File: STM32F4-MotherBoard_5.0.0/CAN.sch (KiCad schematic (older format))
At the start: 0 parts

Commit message: SDとCANの追加とラベルミス修正
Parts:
- added J? (x2): RJ45, symbol RJ45
- added R?: 10k, symbol R
- added U?: MCP2551-I/SN, SO-8, symbol MCP2551-I/SN
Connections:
- net labels added: CAN_RX, CAN_TX, GND
- wire segments 0 -> 47
- no-connect marks 0 -> 1
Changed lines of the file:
@@
 $Descr A4 11693 8268
 encoding utf-8
-Sheet 3 10
+Sheet 3 11
 Title ""
 Date ""
@@
 Comment4 ""
 $EndDescr
+$Comp
+L MCP2551-I/SN U?
+U 1 1 58A2CD9A
+P 5450 3500
+F 0 "U?" H 5050 3850 50  0000 L CNN
+F 1 "MCP2551-I/SN" H 5550 3850 50  0000 L CNN
+F 2 "SO-8" H 5450 3500 50  0000 C CIN
+F 3 "" H 5450 3500 50  0000 C CNN
+	1    5450 3500
+	1    0    0    -1
+$EndComp
+Text GLabel 4500 3400 0    60   Input ~ 0
+CAN_TX
+Text GLabel 4500 3300 0    60   Input ~ 0
+CAN_RX
+Wire Wire Line
+	4500 3300 4950 3300
+Wire Wire Line
+	4950 3400 4500 3400
+$Comp
+L RJ45 J?
+U 1 1 58A2F3E9
+P 7200 2750
+F 0 "J?" H 7400 3250 50  0000 C CNN
+F 1 "RJ45" H 7050 3250 50  0000 C CNN
+F 2 "" H 7200 2750 50  0000 C CNN
+F 3 "" H 7200 2750 50  0000 C CNN
+	1    7200 2750
+	1    0    0    -1
+$EndComp
+Wire Wire Line
+	7450 3400 7450 3200
+Wire Wire Line
+	7350 3200 7350 3250
+Wire Wire Line
+	7350 3250 7250 3250
+Wire Wire Line
+	7250 3250 7250 3200
+Wire Wire Line
+	7300 3250 7300 3700
+Connection ~ 7300 3250
+Wire Wire Line
+	7150 3200 7150 3250
+Wire Wire Line
+	7150 3250 7050 3250
+Wire Wire Line
+	7050 3250 7050 3200
+Wire Wire Line
+	7100 3250 7100 3350
+Wire Wire Line
+	6400 2800 6400 3350
+Connection ~ 7100 3250
+Wire Wire Line
+	6850 3200 6850 3250
+Wire Wire Line
+	6850 3250 6950 3250
+Wire Wire Line
+	6950 3250 6950 3200
+Wire Wire Line
+	6900 3250 6900 3300
+Wire Wire Line
+	6900 3300 6600 3300
+Wire Wire Line
+	6600 3300 6600 2800
+Connection ~ 6900 3250
+Wire Wire Line
+	6400 3350 7100 3350
+Wire Wire Line
+	7550 3200 7550 3600
+Wire Wire Line
+	9100 3600 5950 3600
+$Comp
+L RJ45 J?
+U 1 1 58A2F54B
+P 8750 2750
+F 0 "J?" H 8950 3250 50  0000 C CNN
+F 1 "RJ45" H 8600 3250 50  0000 C CNN
+F 2 "" H 8750 2750 50  0000 C CNN
+F 3 "" H 8750 2750 50  0000 C CNN
+	1    8750 2750
+	1    0    0    -1
+$EndComp
+Wire Wire Line
+	8400 3200 8400 3250
+Wire Wire Line
+	8400 3250 8500 3250
+Wire Wire Line
+	8500 3250 8500 3200
+Wire Wire Line
+	8600 3200 8600 3250
+Wire Wire Line
+	8600 3250 8700 3250
+Wire Wire Line
+	8700 3250 8700 3200
+Wire Wire Line
+	8450 3250 8450 3300
+Wire Wire Line
+	8450 3300 8150 3300
+Wire Wire Line
+	8150 3300 8150 2800
+Connection ~ 8450 3250
+Wire Wire Line
+	8650 3250 8650 3350
+Wire Wire Line
+	8650 3350 7950 3350
+Wire Wire Line
+	7950 3350 7950 2800
+Connection ~ 8650 3250
+Wire Wire Line
+	8800 3200 8800 3250
+Wire Wire Line
+	8800 3250 8900 3250
+Wire Wire Line
+	8900 3250 8900 3200
+Wire Wire Line
+	9000 3200 9000 3400
+Wire Wire Line
+	9100 3200 9100 3600
+Wire Wire Line
+	8850 3250 8850 3700
+Connection ~ 7450 3400
+Connection ~ 8850 3250
+Wire Wire Line
+	9000 3400 5950 3400
+Connection ~ 7550 3600
+$Comp
+L GND #PWR?
+U 1 1 58A2F791
+P 7300 3700
+F 0 "#PWR?" H 7300 3450 50  0001 C CNN
+F 1 "GND" H 7300 3550 50  0000 C CNN
+F 2 "" H 7300 3700 50  0000 C CNN
+F 3 "" H 7300 3700 50  0000 C CNN
+	1    7300 3700
+	1    0    0    -1
+$EndComp
+$Comp
+L GND #PWR?
+U 1 1 58A2F7AB
+P 8850 3700
+F 0 "#PWR?" H 8850 3450 50  0001 C CNN
+F 1 "GND" H 8850 3550 50  0000 C CNN
+F 2 "" H 8850 3700 50  0000 C CNN
+F 3 "" H 8850 3700 50  0000 C CNN
+	1    8850 3700
+	1    0    0    -1
+$EndComp
+Wire Wire Line
+	7800 2450 7800 2400
+Wire Wire Line
+	7800 2400 7750 2400
+Wire Wire Line
+	9300 2400 9350 2400
+Wire Wire Line
+	9350 2400 9350 2450
+$Comp
+L GND #PWR?
+U 1 1 58A2F85E
+P 7800 2450
+F 0 "#PWR?" H 7800 2200 50  0001 C CNN
+F 1 "GND" H 7800 2300 50  0000 C CNN
+F 2 "" H 7800 2450 50  0000 C CNN
+F 3 "" H 7800 2450 50  0000 C CNN
+	1    7800 2450
+	1    0    0    -1
+$EndComp
+$Comp
+L GND #PWR?
+U 1 1 58A2F879
+P 9350 2450
+F 0 "#PWR?" H 9350 2200 50  0001 C CNN
+F 1 "GND" H 9350 2300 50  0000 C CNN
+F 2 "" H 9350 2450 50  0000 C CNN
+F 3 "" H 9350 2450 50  0000 C CNN
+	1    9350 2450
+	1    0    0    -1
+$EndComp
+Wire Wire Line
+	4950 3700 4850 3700
+Wire Wire Line
+	4850 3700 4850 3800
+$Comp
+L R R?
+U 1 1 58A2F8FF
+P 4850 3950
+F 0 "R?" V 4930 3950 50  0000 C CNN
+F 1 "10k" V 4850 3950 50  0000 C CNN
+F 2 "" V 4780 3950 50  0000 C CNN
+F 3 "" H 4850 3950 50  0000 C CNN
+	1    4850 3950
+	1    0    0    -1
+$EndComp
+Wire Wire Line
+	4850 4100 4850 4150
+$Comp
+L GND #PWR?
+U 1 1 58A2F983
+P 4850 4150
+F 0 "#PWR?" H 4850 3900 50  0001 C CNN
+F 1 "GND" H 4850 4000 50  0000 C CNN
+F 2 "" H 4850 4150 50  0000 C CNN
+F 3 "" H 4850 4150 50  0000 C CNN
+	1    4850 4150
+	1    0    0    -1
+$EndComp
+NoConn ~ 4950 3600
 $EndSCHEMATC

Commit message: 回路図終わり
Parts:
- added C20: C, symbol C
- gave numbers to parts that had none: 4
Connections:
- net labels added: +5V
- wire segments 47 -> 53
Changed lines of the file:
@@
 $Descr A4 11693 8268
 encoding utf-8
-Sheet 3 11
+Sheet 3 12
 Title ""
 Date ""
@@
 $EndDescr
 $Comp
-L MCP2551-I/SN U?
+L MCP2551-I/SN U4
 U 1 1 58A2CD9A
 P 5450 3500
-F 0 "U?" H 5050 3850 50  0000 L CNN
+F 0 "U4" H 5050 3850 50  0000 L CNN
 F 1 "MCP2551-I/SN" H 5550 3850 50  0000 L CNN
 F 2 "SO-8" H 5450 3500 50  0000 C CIN
@@
 	4950 3400 4500 3400
 $Comp
-L RJ45 J?
+L RJ45 J1
 U 1 1 58A2F3E9
 P 7200 2750
-F 0 "J?" H 7400 3250 50  0000 C CNN
+F 0 "J1" H 7400 3250 50  0000 C CNN
 F 1 "RJ45" H 7050 3250 50  0000 C CNN
 F 2 "" H 7200 2750 50  0000 C CNN
@@
 	9100 3600 5950 3600
 $Comp
-L RJ45 J?
+L RJ45 J2
 U 1 1 58A2F54B
 P 8750 2750
-F 0 "J?" H 8950 3250 50  0000 C CNN
+F 0 "J2" H 8950 3250 50  0000 C CNN
 F 1 "RJ45" H 8600 3250 50  0000 C CNN
 F 2 "" H 8750 2750 50  0000 C CNN
@@
 Connection ~ 7550 3600
 $Comp
-L GND #PWR?
+L GND #PWR027
 U 1 1 58A2F791
 P 7300 3700
-F 0 "#PWR?" H 7300 3450 50  0001 C CNN
+F 0 "#PWR027" H 7300 3450 50  0001 C CNN
 F 1 "GND" H 7300 3550 50  0000 C CNN
 F 2 "" H 7300 3700 50  0000 C CNN
@@
 $EndComp
 $Comp
-L GND #PWR?
+L GND #PWR028
 U 1 1 58A2F7AB
 P 8850 3700
-F 0 "#PWR?" H 8850 3450 50  0001 C CNN
+F 0 "#PWR028" H 8850 3450 50  0001 C CNN
 F 1 "GND" H 8850 3550 50  0000 C CNN
 F 2 "" H 8850 3700 50  0000 C CNN
@@
 	9350 2400 9350 2450
 $Comp
-L GND #PWR?
+L GND #PWR029
 U 1 1 58A2F85E
 P 7800 2450
-F 0 "#PWR?" H 7800 2200 50  0001 C CNN
+F 0 "#PWR029" H 7800 2200 50  0001 C CNN
 F 1 "GND" H 7800 2300 50  0000 C CNN
 F 2 "" H 7800 2450 50  0000 C CNN
@@
 $EndComp
 $Comp
-L GND #PWR?
+L GND #PWR030
 U 1 1 58A2F879
 P 9350 2450
-F 0 "#PWR?" H 9350 2200 50  0001 C CNN
+F 0 "#PWR030" H 9350 2200 50  0001 C CNN
 F 1 "GND" H 9350 2300 50  0000 C CNN
 F 2 "" H 9350 2450 50  0000 C CNN
@@
 	4850 3700 4850 3800
 $Comp
-L R R?
+L R R7
 U 1 1 58A2F8FF
 P 4850 3950
-F 0 "R?" V 4930 3950 50  0000 C CNN
+F 0 "R7" V 4930 3950 50  0000 C CNN
 F 1 "10k" V 4850 3950 50  0000 C CNN
 F 2 "" V 4780 3950 50  0000 C CNN
@@
 	4850 4100 4850 4150
 $Comp
-L GND #PWR?
+L GND #PWR031
 U 1 1 58A2F983
 P 4850 4150
-F 0 "#PWR?" H 4850 3900 50  0001 C CNN
+F 0 "#PWR031" H 4850 3900 50  0001 C CNN
 F 1 "GND" H 4850 4000 50  0000 C CNN
 F 2 "" H 4850 4150 50  0000 C CNN
@@
 $EndComp
 NoConn ~ 4950 3600
+Wire Wire Line
+	5450 3100 5450 3000
+$Comp
+L +5V #PWR032
+U 1 1 58A58045
+P 5450 3000
+F 0 "#PWR032" H 5450 2850 50  0001 C CNN
+F 1 "+5V" H 5450 3140 50  0000 C CNN
+F 2 "" H 5450 3000 50  0000 C CNN
+F 3 "" H 5450 3000 50  0000 C CNN
+	1    5450 3000
+	1    0    0    -1
+$EndComp
+Wire Wire Line
+	5450 3050 6000 3050
+Wire Wire Line
+	6000 3050 6000 3950
+Connection ~ 5450 3050
+Wire Wire Line
+	6000 3950 5950 3950
+$Comp
+L C C20
+U 1 1 58A5811F
+P 5800 3950
+F 0 "C20" H 5825 4050 50  0000 L CNN
+F 1 "C" H 5825 3850 50  0000 L CNN
+F 2 "" H 5838 3800 50  0000 C CNN
+F 3 "" H 5800 3950 50  0000 C CNN
+	1    5800 3950
+	0    1    1    0
+$EndComp
+Wire Wire Line
+	5650 3950 5450 3950
+Wire Wire Line
+	5450 3900 5450 4000
+Connection ~ 5450 3950
+$Comp
+L GND #PWR033
+U 1 1 58A581D8
+P 5450 4000
+F 0 "#PWR033" H 5450 3750 50  0001 C CNN
+F 1 "GND" H 5450 3850 50  0000 C CNN
+F 2 "" H 5450 4000 50  0000 C CNN
+F 3 "" H 5450 4000 50  0000 C CNN
+	1    5450 4000
+	1    0    0    -1
+$EndComp
 $EndSCHEMATC

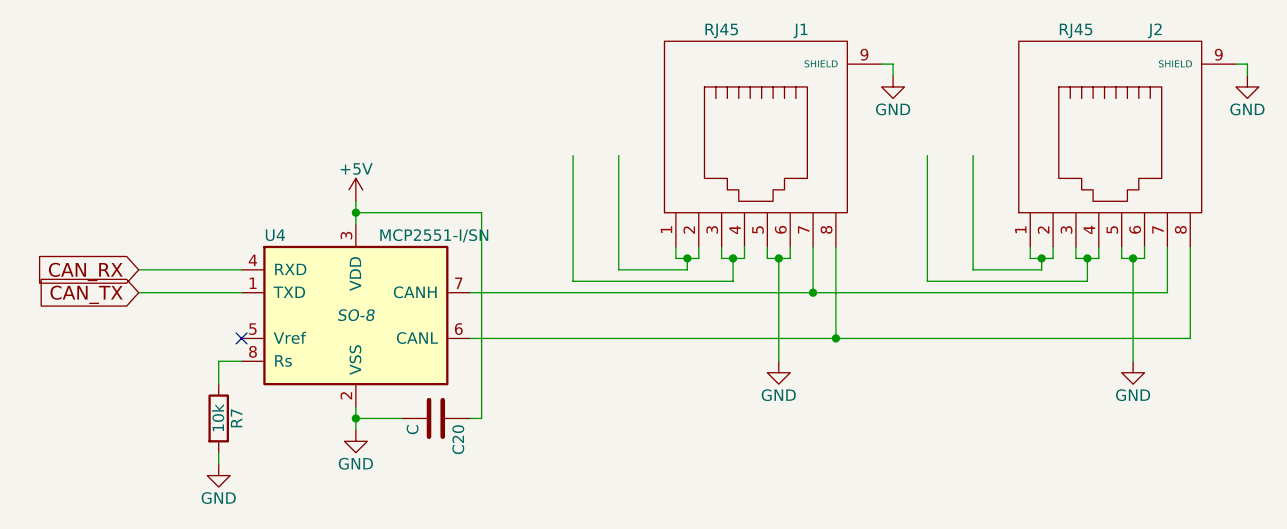
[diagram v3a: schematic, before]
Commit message: 部品名変更
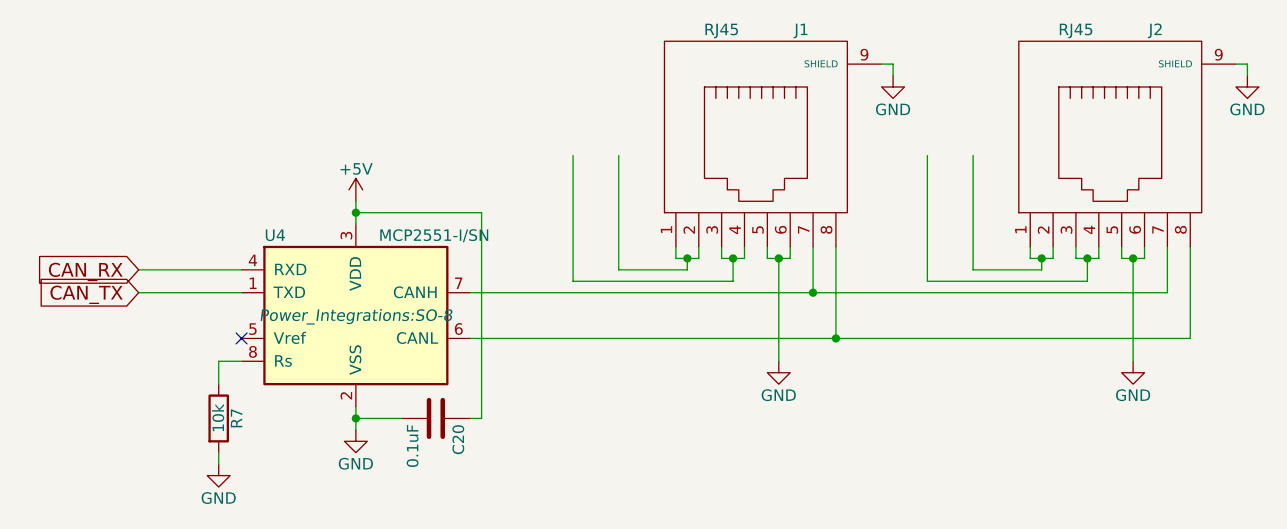
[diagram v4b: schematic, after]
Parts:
- C20: value C -> 0.1uF
- J1, J2: footprint (none) -> robocon_pcb:7810-8P8C
- R7: footprint (none) -> robocon_pcb:SM0603_EXP0.5mm
- U4: footprint SO-8 -> Power_Integrations:SO-8
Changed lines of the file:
@@
 EESchema Schematic File Version 2
+LIBS:STM32F4-MotherBoard_5.0.0-rescue
 LIBS:power
 LIBS:device
@@
 F 0 "U4" H 5050 3850 50  0000 L CNN
 F 1 "MCP2551-I/SN" H 5550 3850 50  0000 L CNN
-F 2 "SO-8" H 5450 3500 50  0000 C CIN
+F 2 "Power_Integrations:SO-8" H 5450 3500 50  0000 C CIN
 F 3 "" H 5450 3500 50  0000 C CNN
 	1    5450 3500
@@
 F 0 "J1" H 7400 3250 50  0000 C CNN
 F 1 "RJ45" H 7050 3250 50  0000 C CNN
-F 2 "" H 7200 2750 50  0000 C CNN
+F 2 "robocon_pcb:7810-8P8C" H 7200 2750 50  0001 C CNN
 F 3 "" H 7200 2750 50  0000 C CNN
 	1    7200 2750
@@
 F 0 "J2" H 8950 3250 50  0000 C CNN
 F 1 "RJ45" H 8600 3250 50  0000 C CNN
-F 2 "" H 8750 2750 50  0000 C CNN
+F 2 "robocon_pcb:7810-8P8C" H 8750 2750 50  0001 C CNN
 F 3 "" H 8750 2750 50  0000 C CNN
 	1    8750 2750
@@
 Connection ~ 7550 3600
 $Comp
-L GND #PWR027
+L GND #PWR029
 U 1 1 58A2F791
 P 7300 3700
-F 0 "#PWR027" H 7300 3450 50  0001 C CNN
+F 0 "#PWR029" H 7300 3450 50  0001 C CNN
 F 1 "GND" H 7300 3550 50  0000 C CNN
 F 2 "" H 7300 3700 50  0000 C CNN
@@
 $EndComp
 $Comp
-L GND #PWR028
+L GND #PWR030
 U 1 1 58A2F7AB
 P 8850 3700
-F 0 "#PWR028" H 8850 3450 50  0001 C CNN
+F 0 "#PWR030" H 8850 3450 50  0001 C CNN
 F 1 "GND" H 8850 3550 50  0000 C CNN
 F 2 "" H 8850 3700 50  0000 C CNN
@@
 	9350 2400 9350 2450
 $Comp
-L GND #PWR029
+L GND #PWR031
 U 1 1 58A2F85E
 P 7800 2450
-F 0 "#PWR029" H 7800 2200 50  0001 C CNN
+F 0 "#PWR031" H 7800 2200 50  0001 C CNN
 F 1 "GND" H 7800 2300 50  0000 C CNN
 F 2 "" H 7800 2450 50  0000 C CNN
@@
 $EndComp
 $Comp
-L GND #PWR030
+L GND #PWR032
 U 1 1 58A2F879
 P 9350 2450
-F 0 "#PWR030" H 9350 2200 50  0001 C CNN
+F 0 "#PWR032" H 9350 2200 50  0001 C CNN
 F 1 "GND" H 9350 2300 50  0000 C CNN
 F 2 "" H 9350 2450 50  0000 C CNN
@@
 F 0 "R7" V 4930 3950 50  0000 C CNN
 F 1 "10k" V 4850 3950 50  0000 C CNN
-F 2 "" V 4780 3950 50  0000 C CNN
+F 2 "robocon_pcb:SM0603_EXP0.5mm" V 4780 3950 50  0001 C CNN
 F 3 "" H 4850 3950 50  0000 C CNN
 	1    4850 3950
@@
 	4850 4100 4850 4150
 $Comp
-L GND #PWR031
+L GND #PWR033
 U 1 1 58A2F983
 P 4850 4150
-F 0 "#PWR031" H 4850 3900 50  0001 C CNN
+F 0 "#PWR033" H 4850 3900 50  0001 C CNN
 F 1 "GND" H 4850 4000 50  0000 C CNN
 F 2 "" H 4850 4150 50  0000 C CNN
@@
 	5450 3100 5450 3000
 $Comp
-L +5V #PWR032
+L +5V #PWR034
 U 1 1 58A58045
 P 5450 3000
-F 0 "#PWR032" H 5450 2850 50  0001 C CNN
+F 0 "#PWR034" H 5450 2850 50  0001 C CNN
 F 1 "+5V" H 5450 3140 50  0000 C CNN
 F 2 "" H 5450 3000 50  0000 C CNN
@@
 P 5800 3950
 F 0 "C20" H 5825 4050 50  0000 L CNN
-F 1 "C" H 5825 3850 50  0000 L CNN
-F 2 "" H 5838 3800 50  0000 C CNN
+F 1 "0.1uF" H 5825 3850 50  0000 L CNN
+F 2 "" H 5838 3800 50  0001 C CNN
 F 3 "" H 5800 3950 50  0000 C CNN
 	1    5800 3950
@@
 Connection ~ 5450 3950
 $Comp
-L GND #PWR033
+L GND #PWR035
 U 1 1 58A581D8
 P 5450 4000
-F 0 "#PWR033" H 5450 3750 50  0001 C CNN
+F 0 "#PWR035" H 5450 3750 50  0001 C CNN
 F 1 "GND" H 5450 3850 50  0000 C CNN
 F 2 "" H 5450 4000 50  0000 C CNN

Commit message: 関連付けできたの
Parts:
- C20: footprint (none) -> robocon_pcb:SM0805_EXP0.5mm
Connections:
- net labels added: +3.3VP, +5VP
- net labels removed: +5V
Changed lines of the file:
@@
 Wire Wire Line
 	5450 3100 5450 3000
-$Comp
-L +5V #PWR034
-U 1 1 58A58045
-P 5450 3000
-F 0 "#PWR034" H 5450 2850 50  0001 C CNN
-F 1 "+5V" H 5450 3140 50  0000 C CNN
-F 2 "" H 5450 3000 50  0000 C CNN
-F 3 "" H 5450 3000 50  0000 C CNN
-	1    5450 3000
-	1    0    0    -1
-$EndComp
 Wire Wire Line
 	5450 3050 6000 3050
@@
 F 0 "C20" H 5825 4050 50  0000 L CNN
 F 1 "0.1uF" H 5825 3850 50  0000 L CNN
-F 2 "" H 5838 3800 50  0001 C CNN
+F 2 "robocon_pcb:SM0805_EXP0.5mm" H 5838 3800 50  0001 C CNN
 F 3 "" H 5800 3950 50  0000 C CNN
 	1    5800 3950
@@
 Connection ~ 5450 3950
 $Comp
-L GND #PWR035
+L GND #PWR034
 U 1 1 58A581D8
 P 5450 4000
-F 0 "#PWR035" H 5450 3750 50  0001 C CNN
+F 0 "#PWR034" H 5450 3750 50  0001 C CNN
 F 1 "GND" H 5450 3850 50  0000 C CNN
 F 2 "" H 5450 4000 50  0000 C CNN
@@
 	1    0    0    -1
 $EndComp
+$Comp
+L +5VP #PWR035
+U 1 1 58A93695
+P 5450 3000
+F 0 "#PWR035" H 5450 2850 50  0001 C CNN
+F 1 "+5VP" H 5450 3140 50  0000 C CNN
+F 2 "" H 5450 3000 50  0000 C CNN
+F 3 "" H 5450 3000 50  0000 C CNN
+	1    5450 3000
+	1    0    0    -1
+$EndComp
+$Comp
+L +5VP #PWR036
+U 1 1 58A936B6
+P 7950 2800
+F 0 "#PWR036" H 7950 2650 50  0001 C CNN
+F 1 "+5VP" H 7950 2940 50  0000 C CNN
+F 2 "" H 7950 2800 50  0000 C CNN
+F 3 "" H 7950 2800 50  0000 C CNN
+	1    7950 2800
+	1    0    0    -1
+$EndComp
+$Comp
+L +5VP #PWR037
+U 1 1 58A936EF
+P 6400 2800
+F 0 "#PWR037" H 6400 2650 50  0001 C CNN
+F 1 "+5VP" H 6400 2940 50  0000 C CNN
+F 2 "" H 6400 2800 50  0000 C CNN
+F 3 "" H 6400 2800 50  0000 C CNN
+	1    6400 2800
+	1    0    0    -1
+$EndComp
+$Comp
+L +3.3VP #PWR038
+U 1 1 58A93706
+P 6600 2800
+F 0 "#PWR038" H 6750 2750 50  0001 C CNN
+F 1 "+3.3VP" H 6600 2900 50  0000 C CNN
+F 2 "" H 6600 2800 50  0000 C CNN
+F 3 "" H 6600 2800 50  0000 C CNN
+	1    6600 2800
+	1    0    0    -1
+$EndComp
+$Comp
+L +3.3VP #PWR039
+U 1 1 58A93727
+P 8150 2800
+F 0 "#PWR039" H 8300 2750 50  0001 C CNN
+F 1 "+3.3VP" H 8150 2900 50  0000 C CNN
+F 2 "" H 8150 2800 50  0000 C CNN
+F 3 "" H 8150 2800 50  0000 C CNN
+	1    8150 2800
+	1    0    0    -1
+$EndComp

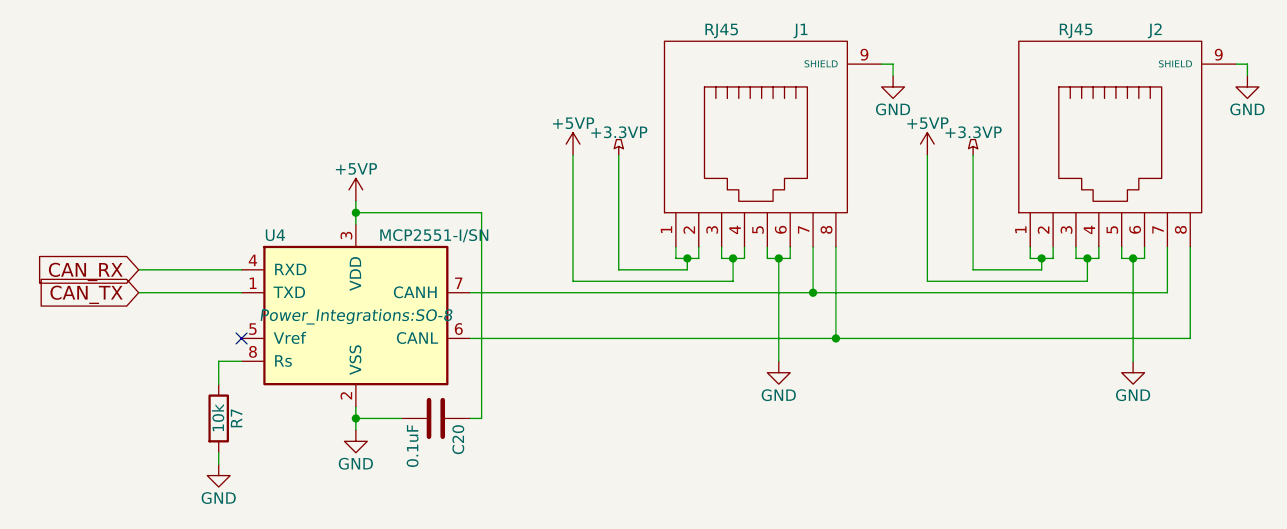
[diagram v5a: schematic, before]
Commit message: 部品配置終わり
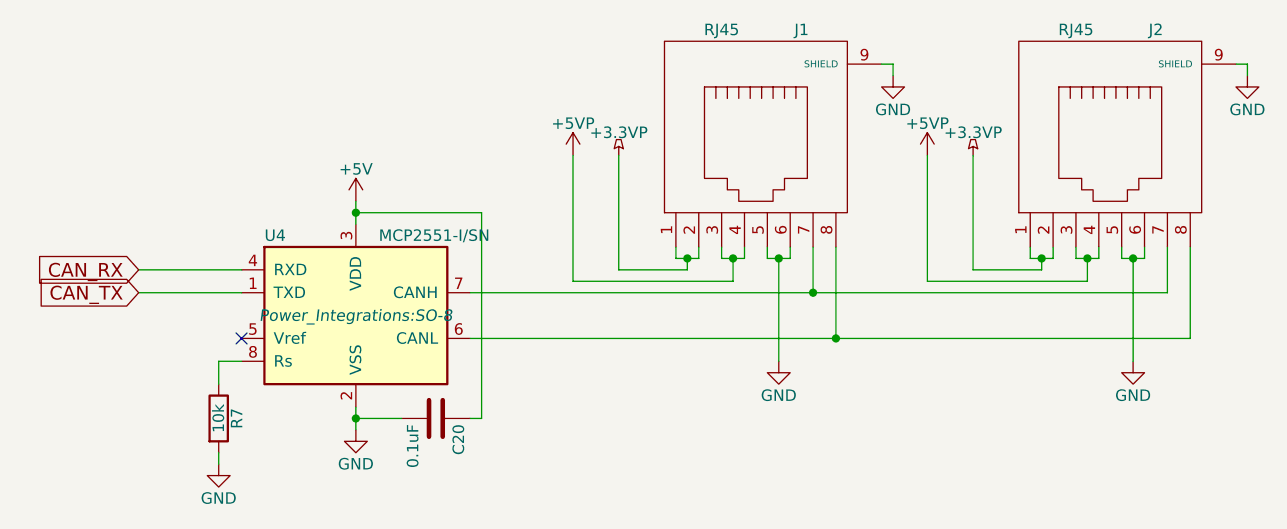
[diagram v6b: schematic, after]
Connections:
- net +5VP: no longer C20.1, U4.3 (VDD)
- new net +5V: C20.1, U4.3 (VDD)
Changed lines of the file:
@@
 $Comp
 L +5VP #PWR035
-U 1 1 58A93695
-P 5450 3000
-F 0 "#PWR035" H 5450 2850 50  0001 C CNN
-F 1 "+5VP" H 5450 3140 50  0000 C CNN
-F 2 "" H 5450 3000 50  0000 C CNN
-F 3 "" H 5450 3000 50  0000 C CNN
-	1    5450 3000
-	1    0    0    -1
-$EndComp
-$Comp
-L +5VP #PWR036
 U 1 1 58A936B6
 P 7950 2800
-F 0 "#PWR036" H 7950 2650 50  0001 C CNN
+F 0 "#PWR035" H 7950 2650 50  0001 C CNN
 F 1 "+5VP" H 7950 2940 50  0000 C CNN
 F 2 "" H 7950 2800 50  0000 C CNN
@@
 $EndComp
 $Comp
-L +5VP #PWR037
+L +5VP #PWR036
 U 1 1 58A936EF
 P 6400 2800
-F 0 "#PWR037" H 6400 2650 50  0001 C CNN
+F 0 "#PWR036" H 6400 2650 50  0001 C CNN
 F 1 "+5VP" H 6400 2940 50  0000 C CNN
 F 2 "" H 6400 2800 50  0000 C CNN
@@
 $EndComp
 $Comp
-L +3.3VP #PWR038
+L +3.3VP #PWR037
 U 1 1 58A93706
 P 6600 2800
-F 0 "#PWR038" H 6750 2750 50  0001 C CNN
+F 0 "#PWR037" H 6750 2750 50  0001 C CNN
 F 1 "+3.3VP" H 6600 2900 50  0000 C CNN
 F 2 "" H 6600 2800 50  0000 C CNN
@@
 $EndComp
 $Comp
-L +3.3VP #PWR039
+L +3.3VP #PWR038
 U 1 1 58A93727
 P 8150 2800
-F 0 "#PWR039" H 8300 2750 50  0001 C CNN
+F 0 "#PWR038" H 8300 2750 50  0001 C CNN
 F 1 "+3.3VP" H 8150 2900 50  0000 C CNN
 F 2 "" H 8150 2800 50  0000 C CNN
@@
 	1    0    0    -1
 $EndComp
+$Comp
+L +5V #PWR039
+U 1 1 58B50836
+P 5450 3000
+F 0 "#PWR039" H 5450 2850 50  0001 C CNN
+F 1 "+5V" H 5450 3140 50  0000 C CNN
+F 2 "" H 5450 3000 50  0000 C CNN
+F 3 "" H 5450 3000 50  0000 C CNN
+	1    5450 3000
+	1    0    0    -1
+$EndComp

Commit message: ミス
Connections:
- net +3.3VP is gone; now on net +5VP: J1.1, J1.2, J2.1, J2.2
- net +5VP: no longer J1.3, J1.4, J2.3, J2.4
- new net +12VA: J1.3, J1.4, J2.3, J2.4
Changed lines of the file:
@@
 L +5VP #PWR035
 U 1 1 58A936B6
-P 7950 2800
-F 0 "#PWR035" H 7950 2650 50  0001 C CNN
-F 1 "+5VP" H 7950 2940 50  0000 C CNN
-F 2 "" H 7950 2800 50  0000 C CNN
-F 3 "" H 7950 2800 50  0000 C CNN
-	1    7950 2800
+P 8150 2800
+F 0 "#PWR035" H 8150 2650 50  0001 C CNN
+F 1 "+5VP" H 8150 2940 50  0000 C CNN
+F 2 "" H 8150 2800 50  0000 C CNN
+F 3 "" H 8150 2800 50  0000 C CNN
+	1    8150 2800
 	1    0    0    -1
 $EndComp
@@
 L +5VP #PWR036
 U 1 1 58A936EF
+P 6600 2800
+F 0 "#PWR036" H 6600 2650 50  0001 C CNN
+F 1 "+5VP" H 6600 2940 50  0000 C CNN
+F 2 "" H 6600 2800 50  0000 C CNN
+F 3 "" H 6600 2800 50  0000 C CNN
+	1    6600 2800
+	1    0    0    -1
+$EndComp
+$Comp
+L +5V #PWR037
+U 1 1 58B50836
+P 5450 3000
+F 0 "#PWR037" H 5450 2850 50  0001 C CNN
+F 1 "+5V" H 5450 3140 50  0000 C CNN
+F 2 "" H 5450 3000 50  0000 C CNN
+F 3 "" H 5450 3000 50  0000 C CNN
+	1    5450 3000
+	1    0    0    -1
+$EndComp
+$Comp
+L +12VA #PWR038
+U 1 1 58CFCDC9
 P 6400 2800
-F 0 "#PWR036" H 6400 2650 50  0001 C CNN
-F 1 "+5VP" H 6400 2940 50  0000 C CNN
+F 0 "#PWR038" H 6400 2650 50  0001 C CNN
+F 1 "+12VA" H 6400 2940 50  0000 C CNN
 F 2 "" H 6400 2800 50  0000 C CNN
 F 3 "" H 6400 2800 50  0000 C CNN
@@
 $EndComp
 $Comp
-L +3.3VP #PWR037
-U 1 1 58A93706
-P 6600 2800
-F 0 "#PWR037" H 6750 2750 50  0001 C CNN
-F 1 "+3.3VP" H 6600 2900 50  0000 C CNN
-F 2 "" H 6600 2800 50  0000 C CNN
-F 3 "" H 6600 2800 50  0000 C CNN
-	1    6600 2800
+L +12VA #PWR039
+U 1 1 58CFCDEA
+P 7950 2800
+F 0 "#PWR039" H 7950 2650 50  0001 C CNN
+F 1 "+12VA" H 7950 2940 50  0000 C CNN
+F 2 "" H 7950 2800 50  0000 C CNN
+F 3 "" H 7950 2800 50  0000 C CNN
+	1    7950 2800
 	1    0    0    -1
 $EndComp
-$Comp
-L +3.3VP #PWR038
-U 1 1 58A93727
-P 8150 2800
-F 0 "#PWR038" H 8300 2750 50  0001 C CNN
-F 1 "+3.3VP" H 8150 2900 50  0000 C CNN
-F 2 "" H 8150 2800 50  0000 C CNN
-F 3 "" H 8150 2800 50  0000 C CNN
-	1    8150 2800
-	1    0    0    -1
-$EndComp
-$Comp
-L +5V #PWR039
-U 1 1 58B50836
-P 5450 3000
-F 0 "#PWR039" H 5450 2850 50  0001 C CNN
-F 1 "+5V" H 5450 3140 50  0000 C CNN
-F 2 "" H 5450 3000 50  0000 C CNN
-F 3 "" H 5450 3000 50  0000 C CNN
-	1    5450 3000
-	1    0    0    -1
-$EndComp
